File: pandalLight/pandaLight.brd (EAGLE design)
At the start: 90 x 57.4 mm, 114 parts, among them J1 PJ-037A, U1 6SLX9TQG144, U2 MIC2230-XXYML, U3 FT2232HL, U4 93LC46BT-I/OT, U5 TPD12S016PWR, U6 TXB0104RGYR, U7 M25P40-VMN, U8 TPD12S016PWR, U9 PAN1322, X1 USBUB-S, X2 HDMI_RECEPTICAL_A, X3 HDMI_RECEPTICAL_A, X4 PMOD-2X6, X5 PMOD-2X6, X6 PLR135-T10, X7 PLT133-T10W, Y1 403, Y2 20Mhz

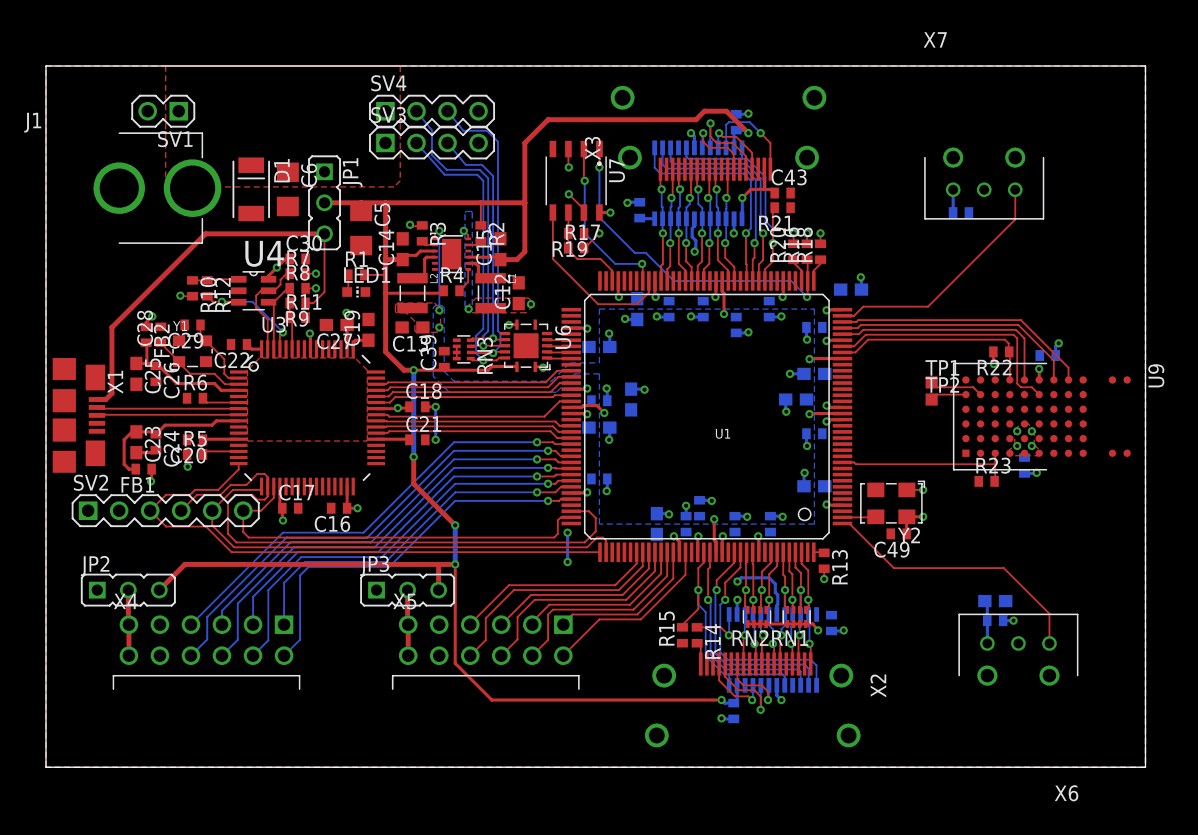
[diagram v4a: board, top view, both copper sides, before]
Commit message: Major design change: I remembered multiboot! That makes it possible to use two HDMI receivers again! So I removed the SPDI/Fs, for which there was no more space, and I added the HDMI receptical and routed all the signals; Added latest BOM
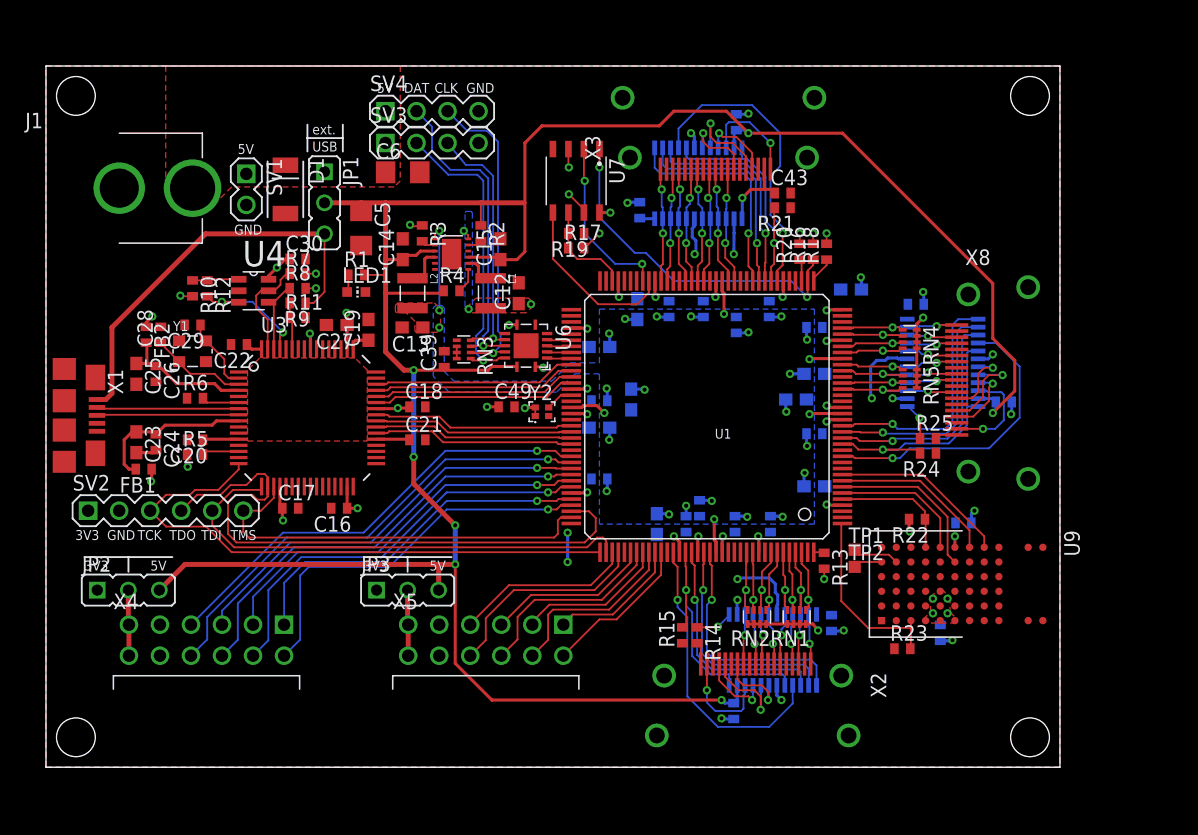
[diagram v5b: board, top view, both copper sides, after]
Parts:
- removed C50, C51: 0.1u, pandaLight:0402
- removed L3: 47u, pandaLight:0603
- removed X6: PLR135-T10, pandaLight:PLR135-T10_PLT133-T10W
- removed X7: PLT133-T10W, pandaLight:PLR135-T10_PLT133-T10W
- added C54, C55: 0.1u, pandaLight:0402
- added R24: 10k, pandaLight:0402
- added R25: 1k, pandaLight:0402
- added RN4, RN5: 51, pandaLight:741C083
- added U10: TPD12S016PWR, pandaLight:PW_R-PDSO-G24
- added X8: HDMI_RECEPTICAL_A, pandaLight:HDMI_TYPE_A_RECEPTICAL
- Y2: device pandaLight:636 -> pandaLight:OSCI-1.6X1.2
- moved C49 33.7 mm to (37.7, 29.5), turned to 0 degrees
- moved Y2 29.6 mm to (40.6, 29.1), turned to 0 degrees
- moved C53 15.3 mm to (75.1, 20.0)
- moved R22 15.3 mm to (71.3, 20.3)
- moved R23 15.3 mm to (70.1, 9.70)
- moved U9 15.3 mm to (75.0, 15.0)
- moved C52 15.3 mm to (73.2, 11.0)
- moved TP2 15.1 mm to (66.2, 16.4)
- moved TP1 15.1 mm to (66.2, 17.8)
- moved C6 9.50 mm to (29.2, 48.7), turned to 0 degrees
- moved SV1 9.34 mm to (16.4, 47.3), turned to 270 degrees
- moved D1 2.80 mm to (19.6, 47.3)
- moved R16 0.50 mm to (62.8, 42.2)
- moved R18 0.50 mm to (63.9, 42.2)
- moved R20 0.50 mm to (61.7, 42.2)
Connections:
- net HDMI_RX_CEC renamed HDMI_RX0_CEC
- net HDMI_RX_CLK_N renamed HDMI_RX0_CLK_N
- net HDMI_RX_CLK_P renamed HDMI_RX0_CLK_P
- net HDMI_RX_DATA0_N renamed HDMI_RX0_DATA0_N
- net HDMI_RX_DATA0_P renamed HDMI_RX0_DATA0_P
- net HDMI_RX_DATA1_N renamed HDMI_RX0_DATA1_N
- net HDMI_RX_DATA1_P renamed HDMI_RX0_DATA1_P
- net HDMI_RX_DATA2_N renamed HDMI_RX0_DATA2_N
- net HDMI_RX_DATA2_P renamed HDMI_RX0_DATA2_P
- net HDMI_RX_SCL_5V renamed HDMI_RX0_SCL
- net HDMI_RX_SDA_5V renamed HDMI_RX0_SDA
- net HDMI_TX_HPD_5V renamed HDMI_TX_HPD
- net HDMI_TX_SCL_5V renamed HDMI_TX_SCL
- net HDMI_TX_SDA_5V renamed HDMI_TX_SDA
- removed net HDMI_RX_CEC_3V3: U1.P132, U5.1
- removed net HDMI_RX_CTRL_EN: R15.2, U1.P126, U5.12, U5.5
- removed net HDMI_RX_SCL_3V3: U1.P131, U5.2
- removed net HDMI_RX_SDA_3V3: U1.P127, U5.3
- removed net N$36: C50.1, L3.2, X6.1
- removed net TOS_IN: U1.P1, X6.3
- removed net TOS_OUT: U1.P35, X7.1
- new net HDMI_RX0_CEC_3V3: U1.P127, U5.1
- new net HDMI_RX0_EN: R15.2, U1.P123, U5.12, U5.5
- new net HDMI_RX0_HPD: U5.10, X2.18
- new net HDMI_RX0_HPD_3V3: U1.P121, U5.4
- new net HDMI_RX0_SCL_3V3: U1.P126, U5.2
- new net HDMI_RX0_SDA_3V3: U1.P124, U5.3
- new net HDMI_RX1_5V: R25.1, U10.13
- new net HDMI_RX1_CEC: U10.7, X8.13
- new net HDMI_RX1_CEC_3V3: U1.P17, U10.1
- new net HDMI_RX1_CLK_N: RN5.4, U1.P23, U10.15, X8.12
- new net HDMI_RX1_CLK_P: RN5.3, U1.P24, U10.16, X8.10
- new net HDMI_RX1_DATA0_N: RN5.2, U1.P26, U10.17, X8.9
- new net HDMI_RX1_DATA0_P: RN5.1, U1.P27, U10.18, X8.7
- new net HDMI_RX1_DATA1_N: RN4.4, U1.P29, U10.20, X8.6
- new net HDMI_RX1_DATA1_P: RN4.3, U1.P30, U10.21, X8.4
- new net HDMI_RX1_DATA2_N: RN4.2, U1.P32, U10.22, X8.3
- new net HDMI_RX1_DATA2_P: RN4.1, U1.P33, U10.23, X8.1
- new net HDMI_RX1_EN: R24.2, U1.P14, U10.12, U10.5
- new net HDMI_RX1_HPD: U10.10, X8.18
- new net HDMI_RX1_HPD_3V3: U1.P12, U10.4
- new net HDMI_RX1_SCL: U10.8, X8.15
- new net HDMI_RX1_SCL_3V3: U1.P16, U10.2
- new net HDMI_RX1_SDA: U10.9, X8.16
- new net HDMI_RX1_SDA_3V3: U1.P15, U10.3
- new net HDMI_TX_HPD_3V3: U1.P43, U8.4
- new net N$2: R25.2, X8.19
- net +3V3: now also C54.1, RN4.5, RN4.6, RN4.7, RN4.8, RN5.5, RN5.6, RN5.7, RN5.8, U10.24; no longer C51.1, L3.1, X7.2
- net +5V: now also C55.1, U10.11
- net BT_CTS: now also U1.P6; no longer U1.P32
- net BT_RESET#: now also U1.P1; no longer U1.P11
- net BT_RTS: now also U1.P9; no longer U1.P34
- net BT_RX: now also U1.P7; no longer U1.P30
- net BT_TX: now also U1.P8; no longer U1.P33
- net BT_WAKE: now also U1.P5; no longer U1.P29
- net FPGA_CLK20: now also U1.P87; no longer U1.P2
- net GND: now also C54.2, C55.2, R24.1, U10.14, U10.19, U10.6, X8.11, X8.14, X8.17, X8.2, X8.5, X8.8; no longer C50.2, C51.2, X6.2, X7.3
- net HDMI_TX_CEC_3V3: now also U1.P47; no longer U1.P48
- net HDMI_TX_CTRL_EN: now also U1.P44; no longer U1.P45
- net HDMI_TX_SCL_3V3: now also U1.P46; no longer U1.P47
- net HDMI_TX_SDA_3V3: now also U1.P45; no longer U1.P46
- net PMOD0_0: now also U1.P104; no longer U1.P102
- net PMOD0_1: now also U1.P101; no longer U1.P100
- net PMOD0_2: now also U1.P99; no longer U1.P98
- net PMOD0_3: now also U1.P97; no longer U1.P95
- net PMOD1_0: now also U1.P105; no longer U1.P104
- net PMOD1_1: now also U1.P102; no longer U1.P101
- net PMOD1_2: now also U1.P100; no longer U1.P99
- net PMOD1_3: now also U1.P98; no longer U1.P97
- net PMOD2_0: now also U1.P118; no longer U1.P121
- net PMOD2_1: now also U1.P116; no longer U1.P119
- net PMOD2_2: now also U1.P114; no longer U1.P117
- net PMOD2_3: now also U1.P111; no longer U1.P115
- net PMOD3_0: now also U1.P119; no longer U1.P123
- net PMOD3_1: now also U1.P117; no longer U1.P120
- net PMOD3_2: now also U1.P115; no longer U1.P118
- net PMOD3_3: now also U1.P112; no longer U1.P116
- net USB_CTS#: now also U1.P92; no longer U1.P88
- net USB_DCD#: now also U1.P83; no longer U1.P84
- net USB_DSR#: now also U1.P84; no longer U1.P85
- net USB_DTR#: now also U1.P85; no longer U1.P87
- net USB_RI#: now also U1.P82; no longer U1.P83
- net USB_RTS#: now also U1.P93; no longer U1.P92
- net USB_RXD: now also U1.P94; no longer U1.P93
- net USB_TXD: now also U1.P95; no longer U1.P94
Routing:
- net +5V: track 168.8 -> 208.5 mm, vias 6 -> 7
- net HDMI_TX_HPD_3V3: track 0.00 -> 24.7 mm, vias 0 -> 1
- net HDMI_RX1_HPD_3V3: track 0.00 -> 24.3 mm, vias 0 -> 1
- net HDMI_RX0_HPD_3V3: track 0.00 -> 24.2 mm, vias 0 -> 1
- net TOS_IN: track 22.4 -> 0.00 mm
- net HDMI_RX1_EN: track 0.00 -> 22.2 mm, vias 0 -> 1
- net HDMI_RX0_EN: track 0.00 -> 21.8 mm, vias 0 -> 1
- net HDMI_RX_CTRL_EN: track 21.3 -> 0.00 mm, vias 1 -> 0
- net TOS_OUT: track 19.8 -> 0.00 mm
- net HDMI_RX1_CEC_3V3: track 0.00 -> 19.7 mm, vias 0 -> 1
- net HDMI_RX0_CEC_3V3: track 0.00 -> 19.5 mm, vias 0 -> 1
- net HDMI_RX1_SCL_3V3: track 0.00 -> 19.2 mm, vias 0 -> 1
- net HDMI_RX0_SCL_3V3: track 0.00 -> 19.0 mm, vias 0 -> 1
- net HDMI_RX1_SDA_3V3: track 0.00 -> 19.0 mm, vias 0 -> 1
- net HDMI_RX_CEC_3V3: track 18.8 -> 0.00 mm, vias 1 -> 0
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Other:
- board size 90 x 57.4 mm -> 83 x 57.4 mm
- board text added: "3V3"
- board text added: "5V"
- board text added: "CLK"
- board text added: "DAT"
- board text added: "GND"
- board text added: "TCK"
- board text added: "TDI"
- board text added: "TDO"
- board text added: "TMS"
- board text added: "USB"
- board text added: "ext."

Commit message: Added Feducias; Added logos; Minor silkscreen changes
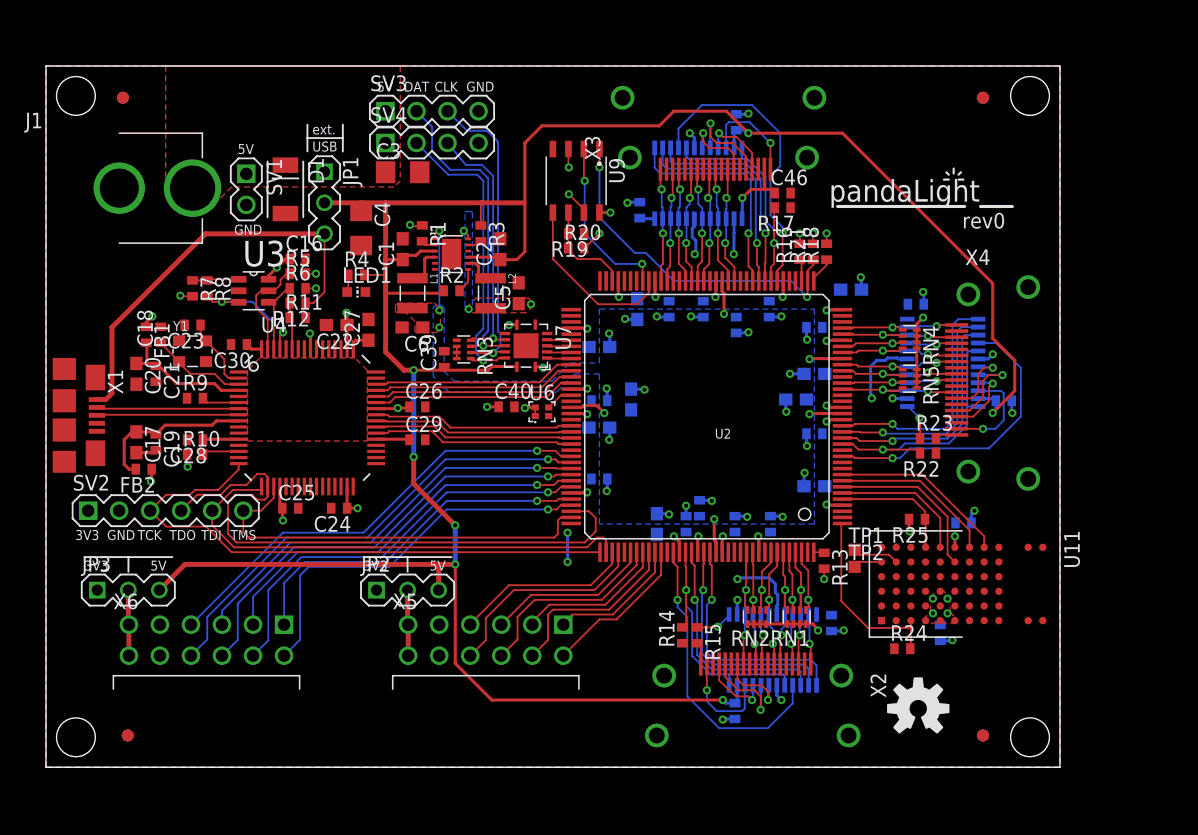
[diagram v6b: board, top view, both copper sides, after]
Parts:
- removed C55: 0.1u, pandaLight:0402
- removed X8: HDMI_RECEPTICAL_A, pandaLight:HDMI_TYPE_A_RECEPTICAL
- removed Y2: 20Mhz, pandaLight:OSCI-1.6X1.2
- added C50: 0.1u, pandaLight:0402
- added FID1, FID2, FID3, FID4, FID5, FID6, FID7, FID8: FIDUCIAL1X2, pandaLight:FIDUCIAL-1X2
- added OSHW-LOGO: (no value), pandaLight:OSHW-LOGO-M
- added U11: PAN1322, pandaLight:PAN1322
- added X6: PMOD-2X6, pandaLight:PMOD-2X6
- C10, C11, C41, C47: value 0.47u -> 4.7u; device pandaLight:0402 -> pandaLight:0603
- C12, C13: value 10u -> 0.47u; device pandaLight:0603 -> pandaLight:0402
- C14, C15: value 4.7u -> 0.47u; device pandaLight:0603 -> pandaLight:0402
- C17, C20, C22: value 0.1u -> 4.7u; device pandaLight:0402 -> pandaLight:0603
- C18: value 0.1u -> 27p
- C19, C25, C40, C46: value 4.7u -> 0.1u; device pandaLight:0603 -> pandaLight:0402
- C23: value 4.7u -> 27p; device pandaLight:0603 -> pandaLight:0402
- C28, C29: value 27p -> 0.1u
- C3, C4: value 0.47u -> 100u; device pandaLight:0402 -> pandaLight:1206
- C43, C49: value 0.1u -> 0.47u
- C5, C6: value 100u -> 10u; device pandaLight:1206 -> pandaLight:0603
- JP2: value PMOD0-1_VCC_SEL -> PMOD2-3_VCC_SEL
- JP3: value PMOD2-3_VCC_SEL -> PMOD0-1_VCC_SEL
- R1: value 1k -> 100k
- R12: value 2.2k -> 4.7k
- R14, R25: value 1k -> 10k
- R15: value 10k -> 1k
- R16: value 2.4k -> 4.7k
- R17: value 100 -> 10k
- R20: value 4.7k -> 100
- R21: value 10k -> 2.4k
- R23: value 4.7k -> 1k
- R24: value 10k -> 4.7k
- R4: value 100k -> 1k
- R6: value 12k -> 10k
- R8: value 10k -> 2.2k
- R9: value 4.7k -> 12k
- U1: value 6SLX9TQG144 -> MIC2230-XXYML; device pandaLight:TQ144 -> pandaLight:MLF-12
- U2: value MIC2230-XXYML -> 6SLX9TQG144; device pandaLight:MLF-12 -> pandaLight:TQ144
- U3: value FT2232HL -> 93LC46BT-I/OT; device pandaLight:LQFP64 -> pandaLight:SOT23-6
- U4: value 93LC46BT-I/OT -> FT2232HL; device pandaLight:SOT23-6 -> pandaLight:LQFP64
- U6: value TXB0104RGYR -> 20Mhz; device pandaLight:S-PVQFN-N14 -> pandaLight:OSCI-1.6X1.2
- U7: value M25P40-VMN -> TXB0104RGYR; device pandaLight:SO8N -> pandaLight:S-PVQFN-N14
- U9: value PAN1322 -> M25P40-VMN; device pandaLight:PAN1322 -> pandaLight:SO8N
- X4: value PMOD-2X6 -> HDMI_RECEPTICAL_A; device pandaLight:PMOD-2X6 -> pandaLight:HDMI_TYPE_A_RECEPTICAL
- moved X4 68.7 mm to (78.5, 31.7)
- moved U9 45.7 mm to (43.4, 48.0)
- moved C4 35.9 mm to (25.8, 44.1), flipped to the top, turned to 270 degrees
- moved C14 32.2 mm to (53.5, 21.2), flipped to the bottom
- moved C3 30.0 mm to (29.2, 48.7), flipped to the top, turned to 0 degrees
- moved C15 29.6 mm to (56.4, 19.9), flipped to the bottom
- moved C2 27.1 mm to (37.2, 42.4), flipped to the top, turned to 90 degrees
- moved C49 26.0 mm to (62.9, 36.0), flipped to the bottom
- moved U1 24.8 mm to (33.2, 42.0), turned to 0 degrees
- moved U2 24.8 mm to (54.1, 28.7), turned to 180 degrees
- moved C46 24.1 mm to (60.3, 47.0), flipped to the top
- moved C13 23.8 mm to (53.8, 37.5), flipped to the bottom, turned to 270 degrees
- moved C9 23.5 mm to (65.9, 39.1)
- moved JP2 22.9 mm to (29.6, 14.5)
- moved JP3 22.9 mm to (6.74, 14.5)
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- renumbered C54 to C51
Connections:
- net +1V2: now also C10.1, C12.1, C14.1, C6.1, C8.1, L1.2, U1.1, U2.P128, U2.P19, U2.P28, U2.P52, U2.P89; no longer C1.1, C13.1, C2.1, C3.1, C4.1, L2.2, U1.P128, U1.P19, U1.P28, U1.P52, U1.P89, U2.1
- net +1V8: now also C27.1, C28.1, C29.1, C30.1, U4.12, U4.37, U4.49, U4.64; no longer C19.1, C20.1, C21.1, C22.1, U3.12, U3.37, U3.49, U3.64
- net +3V3: now also C13.1, C15.1, C22.1, C24.1, C25.1, C26.1, C43.1, C5.1, L2.2, R1.1, R10.1, R21.2, R25.2, R5.2, R6.2, U1.12, U11.A4, U11.A5, U11.A6, U11.B5, U11.C5, U11.F6, U2.P103, U2.P122, U2.P125, U2.P129, U2.P135, U2.P18, U2.P20, U2.P31, U2.P36, U2.P4, U2.P42, U2.P53, U2.P63, U2.P69, U2.P76, U2.P86, U2.P90, U3.6, U4.20, U4.31, U4.42, U4.50, U4.56, U6.4, U7.1, U9.3, U9.7, U9.8; no longer C10.1, C12.1, C17.1, C18.1, C27.1, C30.1, C46.1, C8.1, L1.2, R10.2, R17.2, R22.2, R3.1, R5.1, R8.2, U1.P103, U1.P122, U1.P125, U1.P129, U1.P135, U1.P18, U1.P20, U1.P31, U1.P36, U1.P4, U1.P42, U1.P53, U1.P63, U1.P69, U1.P76, U1.P86, U1.P90, U2.12, U3.20, U3.31, U3.42, U3.50, U3.56, U4.6, U6.8, U7.3, U7.7, U9.A4, U9.A5, U9.A6, U9.B5, U9.C5, U9.F6, Y2.1, Y2.4
- net +5V: now also C1.1, C2.1, C4.1, C50.1, R3.1, R4.2, U1.3, U1.9, U7.14; no longer C14.1, C15.1, C5.1, C55.1, R1.2, R4.1, U2.3, U2.9, U6.14
- net 5V_SUP: now also C3.1; no longer C6.1
- net BT_CTS: now also U11.F5, U2.P6; no longer U1.P6, U9.F5
- net BT_RESET#: now also R24.2, U11.A3, U2.P1; no longer R23.2, U1.P1, U9.A3
- net BT_RTS: now also U11.F8, U2.P9; no longer U1.P9, U9.F8
- net BT_RX: now also U11.E6, U2.P7; no longer U1.P7, U9.E6
- net BT_TX: now also U11.F7, U2.P8; no longer U1.P8, U9.F7
- net BT_WAKE: now also R25.1, U11.F4, U2.P5; no longer R22.1, U1.P5, U9.F4
- net FPGA_CLK20: now also U2.P87, U6.3; no longer U1.P87, Y2.3
- net GND: now also C50.2, R14.1, R17.1, R22.1, R9.1, U1.5, U1.6, U1.EP, U11.A1, U11.A11, U11.A12, U11.A7, U11.A9, U11.C8, U11.C9, U11.D7, U11.D8, U11.E8, U11.E9, U11.F1, U11.F11, U11.F12, U11.F9, U2.P108, U2.P113, U2.P13, U2.P130, U2.P136, U2.P25, U2.P3, U2.P49, U2.P54, U2.P60, U2.P68, U2.P73, U2.P77, U2.P91, U2.P96, U3.2, U4.1, U4.10, U4.11, U4.13, U4.15, U4.25, U4.35, U4.47, U4.5, U4.51, U6.2, U7.7, U7.EP, U9.4, X4.14, X4.17, X4.2, X4.8, X6.11, X6.5; no longer C55.2, R15.1, R21.1, R23.1, R6.1, U1.P108, U1.P113, U1.P13, U1.P130, U1.P136, U1.P25, U1.P3, U1.P49, U1.P54, U1.P60, U1.P68, U1.P73, U1.P77, U1.P91, U1.P96, U2.5, U2.6, U2.EP, U3.1, U3.10, U3.11, U3.13, U3.15, U3.25, U3.35, U3.47, U3.5, U3.51, U4.2, U6.7, U6.EP, U7.4, U9.A1, U9.A11, U9.A12, U9.A7, U9.A9, U9.C8, U9.C9, U9.D7, U9.D8, U9.E8, U9.E9, U9.F1, U9.F11, U9.F12, U9.F9, X8.11, X8.14, X8.17, X8.2, X8.5, X8.8, Y2.2
- net HDMI_RX0_CEC_3V3: now also U2.P127; no longer U1.P127
- net HDMI_RX0_CLK_N: now also U2.P133; no longer U1.P133
- net HDMI_RX0_CLK_P: now also U2.P134; no longer U1.P134
- net HDMI_RX0_DATA0_N: now also U2.P137; no longer U1.P137
- net HDMI_RX0_DATA0_P: now also U2.P138; no longer U1.P138
- net HDMI_RX0_DATA1_N: now also U2.P139; no longer U1.P139
- net HDMI_RX0_DATA1_P: now also U2.P140; no longer U1.P140
- net HDMI_RX0_DATA2_N: now also U2.P141; no longer U1.P141
- net HDMI_RX0_DATA2_P: now also U2.P142; no longer U1.P142
- net HDMI_RX0_EN: now also R14.2, U2.P123; no longer R15.2, U1.P123
- net HDMI_RX0_HPD_3V3: now also U2.P121; no longer U1.P121
- net HDMI_RX0_SCL_3V3: now also U2.P126; no longer U1.P126
- net HDMI_RX0_SDA_3V3: now also U2.P124; no longer U1.P124
- net HDMI_RX1_5V: now also R23.1; no longer R25.1
- net HDMI_RX1_CEC: now also X4.13; no longer X8.13
- net HDMI_RX1_CEC_3V3: now also U2.P17; no longer U1.P17
- net HDMI_RX1_CLK_N: now also U2.P23, X4.12; no longer U1.P23, X8.12
- net HDMI_RX1_CLK_P: now also U2.P24, X4.10; no longer U1.P24, X8.10
- net HDMI_RX1_DATA0_N: now also U2.P26, X4.9; no longer U1.P26, X8.9
- net HDMI_RX1_DATA0_P: now also U2.P27, X4.7; no longer U1.P27, X8.7
- net HDMI_RX1_DATA1_N: now also U2.P29, X4.6; no longer U1.P29, X8.6
- net HDMI_RX1_DATA1_P: now also U2.P30, X4.4; no longer U1.P30, X8.4
- net HDMI_RX1_DATA2_N: now also U2.P32, X4.3; no longer U1.P32, X8.3
- net HDMI_RX1_DATA2_P: now also U2.P33, X4.1; no longer U1.P33, X8.1
- net HDMI_RX1_EN: now also R22.2, U2.P14; no longer R24.2, U1.P14
- net HDMI_RX1_HPD: now also X4.18; no longer X8.18
- net HDMI_RX1_HPD_3V3: now also U2.P12; no longer U1.P12
- net HDMI_RX1_SCL: now also X4.15; no longer X8.15
- net HDMI_RX1_SCL_3V3: now also U2.P16; no longer U1.P16
- net HDMI_RX1_SDA: now also X4.16; no longer X8.16
- net HDMI_RX1_SDA_3V3: now also U2.P15; no longer U1.P15
- net HDMI_RX_5V: now also R15.1; no longer R14.1
- net HDMI_TX_5V: now also C46.1; no longer C43.1
- net HDMI_TX_CEC_3V3: now also U2.P47; no longer U1.P47
- net HDMI_TX_CLK_N: now also U2.P50; no longer U1.P50
- net HDMI_TX_CLK_P: now also U2.P51; no longer U1.P51
- net HDMI_TX_CTRL_EN: now also R17.2, U2.P44; no longer R21.2, U1.P44
- net HDMI_TX_DATA0_N: now also U2.P55; no longer U1.P55
- net HDMI_TX_DATA0_P: now also U2.P56; no longer U1.P56
- net HDMI_TX_DATA1_N: now also U2.P57; no longer U1.P57
- net HDMI_TX_DATA1_P: now also U2.P58; no longer U1.P58
- net HDMI_TX_DATA2_N: now also U2.P61; no longer U1.P61
- net HDMI_TX_DATA2_P: now also U2.P62; no longer U1.P62
- net HDMI_TX_HPD_3V3: now also U2.P43; no longer U1.P43
- net HDMI_TX_SCL_3V3: now also U2.P46; no longer U1.P46
- net HDMI_TX_SDA_3V3: now also U2.P45; no longer U1.P45
- net LEDS0_CLK: now also U2.P78, U7.5; no longer U1.P78, U6.5
- net LEDS0_CLK_5V: now also SV4.3, U7.10; no longer SV3.3, U6.10
- net LEDS0_DATA: now also U2.P81, U7.2; no longer U1.P81, U6.2
- net LEDS0_DATA_5V: now also SV4.2, U7.13; no longer SV3.2, U6.13
- net LEDS1_CLK: now also U2.P80, U7.3; no longer U1.P80, U6.3
- net LEDS1_CLK_5V: now also SV3.3, U7.12; no longer SV4.3, U6.12
- net LEDS1_DATA: now also U2.P79, U7.4; no longer U1.P79, U6.4
- net LEDS1_DATA_5V: now also SV3.2, U7.11; no longer SV4.2, U6.11
- net N$1: now also C23.1, U4.2; no longer C29.1, U3.2
- net N$10: now also R8.2, U3.3, U4.61; no longer R12.2, U3.61, U4.3
- net N$11: now also R9.2, U4.6; no longer R6.2, U3.6
- net N$12: now also R7.1, R8.1, U3.1; no longer R10.1, R12.1, U4.1
- net N$13: now also R10.2, U4.14; no longer R5.2, U3.14
- net N$19: now also U11.E1; no longer U9.E1
- net N$2: now also R23.2, X4.19; no longer R25.2, X8.19
- net N$25: now also R3.2, U1.11; no longer R2.2, U2.11
- net N$27: now also R1.2, U1.2; no longer R3.2, U2.2
- net N$28: now also C20.1, C21.1, FB1.2, U4.4; no longer C25.1, C26.1, FB2.2, U3.4
- net N$29: now also U11.E2; no longer U9.E2
- net N$31: now also C17.1, C19.1, FB2.2, U4.9; no longer C23.1, C24.1, FB1.2, U3.9
- net N$34: now also U2.P37; no longer U1.P37
- net N$35: now also U2.P144; no longer U1.P144
- net N$39: now also R16.1, U2.P39; no longer R20.1, U1.P39
- net N$4: now also R2.2, U1.7; no longer R4.2, U2.7
- net N$40: now also U2.P64, U9.5; no longer U1.P64, U7.5
- net N$41: now also R21.1, U2.P38, U9.1; no longer R16.1, U1.P38, U7.1
- net N$42: now also R20.1, U2.P70, U9.6; no longer R17.1, U1.P70, U7.6
- net N$43: now also U2.P65, U9.2; no longer U1.P65, U7.2
- net N$47: now also R4.1; no longer R1.1
- net N$49: now also JP2.2; no longer JP3.2
- net N$5: now also C18.1, U4.3; no longer C28.1, U3.3
- net N$50: now also R15.2; no longer R14.2
- net N$51: now also JP3.2, X6.12, X6.6; no longer JP2.2, X4.12, X4.6
- net N$6: now also R5.1, U3.5, U4.63; no longer R7.1, U3.63, U4.5
- net N$7: now also U4.7; no longer U3.7
- net N$8: now also U4.8; no longer U3.8
- net N$9: now also R6.1, U3.4, U4.62; no longer R8.1, U3.62, U4.4
- net PMOD0_0: now also U2.P104, X6.1; no longer U1.P104, X4.1
- net PMOD0_1: now also U2.P101, X6.2; no longer U1.P101, X4.2
- net PMOD0_2: now also U2.P99, X6.3; no longer U1.P99, X4.3
- net PMOD0_3: now also U2.P97, X6.4; no longer U1.P97, X4.4
- net PMOD1_0: now also U2.P105, X6.7; no longer U1.P105, X4.7
- net PMOD1_1: now also U2.P102, X6.8; no longer U1.P102, X4.8
- net PMOD1_2: now also U2.P100, X6.9; no longer U1.P100, X4.9
- net PMOD1_3: now also U2.P98, X6.10; no longer U1.P98, X4.10
- net PMOD2_0: now also U2.P118; no longer U1.P118
- net PMOD2_1: now also U2.P116; no longer U1.P116
- net PMOD2_2: now also U2.P114; no longer U1.P114
- net PMOD2_3: now also U2.P111; no longer U1.P111
- net PMOD3_0: now also U2.P119; no longer U1.P119
- net PMOD3_1: now also U2.P117; no longer U1.P117
- net PMOD3_2: now also U2.P115; no longer U1.P115
- net PMOD3_3: now also U2.P112; no longer U1.P112
- net SW1: now also L2.1, U1.8; no longer L1.1, U2.8
- net SW2: now also L1.1, U1.4; no longer L2.1, U2.4
- net USB_CTS#: now also U2.P92, U4.41; no longer U1.P92, U3.41
- net USB_DCD#: now also U2.P83, U4.45; no longer U1.P83, U3.45
- net USB_DSR#: now also U2.P84, U4.44; no longer U1.P84, U3.44
- net USB_DTR#: now also U2.P85, U4.43; no longer U1.P85, U3.43
- net USB_PWRSAVE#: now also R12.2, U4.59; no longer R9.2, U3.59
- net USB_RI#: now also U2.P82, U4.46; no longer U1.P82, U3.46
- net USB_RTS#: now also U2.P93, U4.40; no longer U1.P93, U3.40
- net USB_RXD: now also U2.P94, U4.39; no longer U1.P94, U3.39
- net USB_TCK: now also U2.P109, U4.16; no longer U1.P109, U3.16
- net USB_TDI: now also U2.P110, U4.17; no longer U1.P110, U3.17
- net USB_TDO: now also U2.P106, U4.18; no longer U1.P106, U3.18
- net USB_TMS: now also U2.P107, U4.19; no longer U1.P107, U3.19
- net USB_TXD: now also U2.P95, U4.38; no longer U1.P95, U3.38
- net USB_VBUS: now also R12.1; no longer R9.1
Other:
- board text added: "pandaLight"
- board text added: "rev0"

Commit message: Adjusted and placed part names; refreshed BOM
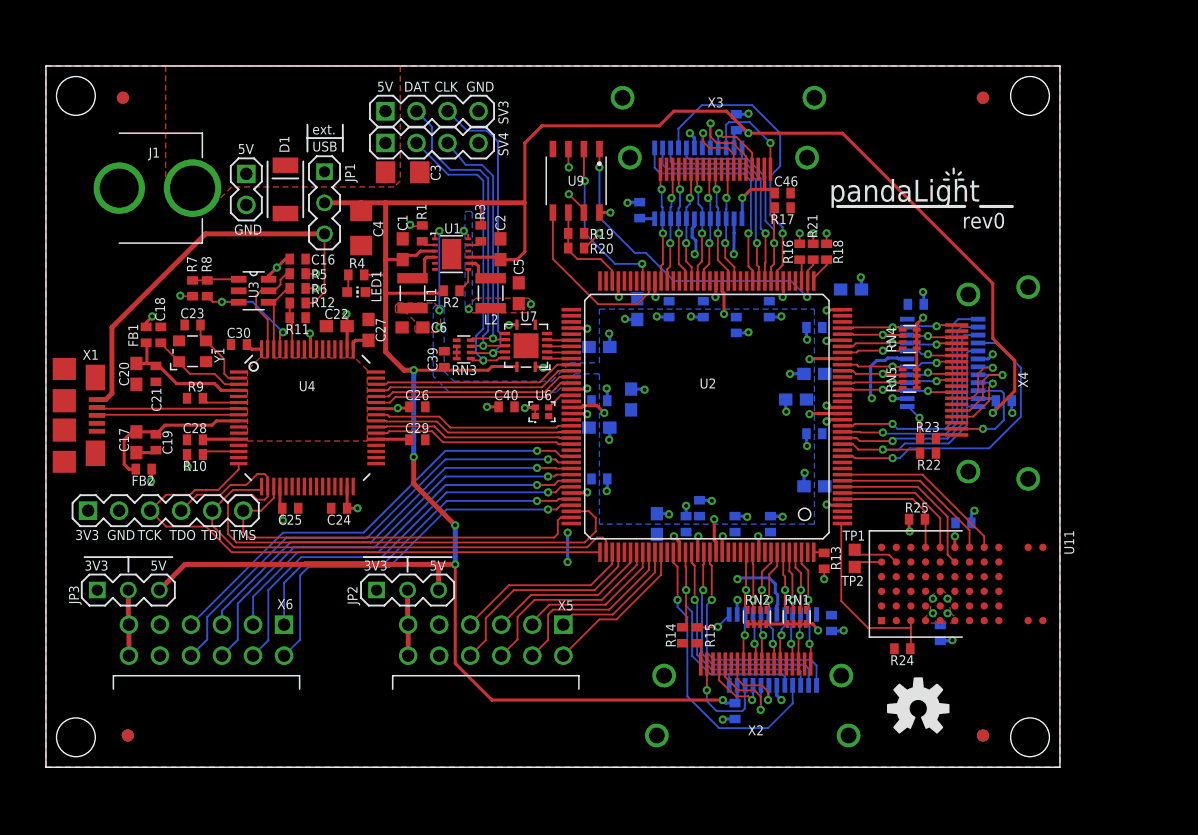
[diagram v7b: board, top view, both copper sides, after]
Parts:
- moved C22 0.10 mm to (23.8, 36.1)
